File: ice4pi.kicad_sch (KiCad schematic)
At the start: 33 parts, among them J1 Conn_02x03, J2 Raspberry_Pi_2_3, J3 USB_C_Receptacle_USB2.0, J4 RJ45_Abracon_ARJP11A-MASA-B-A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, U1 ENC28J60x-SS, U2 DSC1001DE1-025.0000, U3 TPS2375-1

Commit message: fix: led
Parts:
- added R12: 332K, Resistor_SMD:R_0402_1005Metric, symbol Device:R
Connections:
- net LEDA: now also R6.1; no longer R7.1
- net LEDB: now also R7.1; no longer R6.1
- net at J4.11: now also R6.2; no longer R7.2
- net at J4.13: now also R7.2; no longer R6.2
- net at LSI-U1.6 (S2): now also R12.2; no longer U3.6 (PG)
- new net: R12.1, U3.6 (PG)
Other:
- moved on the sheet: R6, R7
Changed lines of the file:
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@@
 	(wire
 		(pts
-			(xy 106.68 96.52) (xy 113.03 96.52)
+			(xy 106.68 106.68) (xy 113.03 106.68)
 		)
 		(stroke
@@
 	(wire
 		(pts
-			(xy 96.52 106.68) (xy 99.06 106.68)
+			(xy 39.37 53.34) (xy 62.23 53.34)
 		)
 		(stroke
@@
 	(wire
 		(pts
-			(xy 39.37 53.34) (xy 62.23 53.34)
+			(xy 96.52 109.22) (xy 107.95 109.22)
 		)
 		(stroke
@@
 	(wire
 		(pts
-			(xy 107.95 99.06) (xy 96.52 99.06)
+			(xy 203.2 50.8) (xy 203.2 53.34)
 		)
 		(stroke
@@
 	(wire
 		(pts
-			(xy 203.2 50.8) (xy 203.2 53.34)
+			(xy 39.37 99.06) (xy 53.34 99.06)
 		)
 		(stroke
@@
 	(wire
 		(pts
-			(xy 39.37 99.06) (xy 53.34 99.06)
+			(xy 71.12 147.32) (xy 76.2 147.32)
 		)
 		(stroke
@@
 	(wire
 		(pts
-			(xy 71.12 147.32) (xy 76.2 147.32)
+			(xy 203.2 53.34) (xy 203.2 55.88)
 		)
 		(stroke
@@
 	(wire
 		(pts
-			(xy 203.2 53.34) (xy 203.2 55.88)
+			(xy 142.24 96.52) (xy 157.48 96.52)
 		)
 		(stroke
@@
 	(wire
 		(pts
-			(xy 142.24 96.52) (xy 157.48 96.52)
+			(xy 205.74 104.14) (xy 208.28 104.14)
 		)
 		(stroke
@@
 	(wire
 		(pts
+			(xy 96.52 99.06) (xy 107.95 99.06)
+		)
+		(stroke
+			(width 0)
+			(type default)
+		)
+	)
+	(wire
+		(pts
 			(xy 58.42 60.96) (xy 62.23 60.96)
 		)
@@
 	(wire
 		(pts
-			(xy 106.68 106.68) (xy 113.03 106.68)
+			(xy 106.68 96.52) (xy 113.03 96.52)
 		)
 		(stroke
@@
 	(wire
 		(pts
-			(xy 96.52 96.52) (xy 99.06 96.52)
-		)
-		(stroke
-			(width 0)
-			(type default)
-		)
-	)
-	(wire
-		(pts
 			(xy 203.2 45.72) (xy 203.2 48.26)
 		)
@@
 	(wire
 		(pts
+			(xy 96.52 106.68) (xy 99.06 106.68)
+		)
+		(stroke
+			(width 0)
+			(type default)
+		)
+	)
+	(wire
+		(pts
 			(xy 58.42 148.59) (xy 58.42 149.86)
 		)
@@
 	(wire
 		(pts
-			(xy 107.95 109.22) (xy 96.52 109.22)
-		)
-		(stroke
-			(width 0)
-			(type default)
-		)
-	)
-	(wire
-		(pts
 			(xy 203.2 43.18) (xy 203.2 45.72)
 		)
@@
 	(wire
 		(pts
-			(xy 195.58 104.14) (xy 208.28 104.14)
+			(xy 195.58 104.14) (xy 198.12 104.14)
 		)
 		(stroke
@@
 		)
 	)
+	(wire
+		(pts
+			(xy 96.52 96.52) (xy 99.06 96.52)
+		)
+		(stroke
+			(width 0)
+			(type default)
+		)
+	)
 	(text_box "INTERFACE"
 		(exclude_from_sim no)
@@
 		)
 	)
-	(label "LEDB"
-		(at 107.95 96.52 0)
+	(label "LEDA"
+		(at 109.22 106.68 0)
 		(fields_autoplaced yes)
 		(effects
@@
 		)
 	)
-	(label "LEDA"
-		(at 107.95 106.68 0)
+	(label "LEDB"
+		(at 109.22 96.52 0)
 		(fields_autoplaced yes)
 		(effects
@@
 	(symbol
 		(lib_id "power:GND")
-		(at 107.95 99.06 90)
+		(at 107.95 109.22 90)
 		(unit 1)
 		(exclude_from_sim no)
@@
 		(dnp no)
 		(property "Reference" "#PWR06"
-			(at 114.3 99.06 0)
+			(at 114.3 109.22 0)
 			(effects
 				(font
@@
 		)
 		(property "Value" "GND"
-			(at 110.49 97.79 90)
+			(at 110.49 107.95 90)
 			(effects
 				(font
@@
 		)
 		(property "Footprint" ""
-			(at 107.95 99.06 0)
+			(at 107.95 109.22 0)
 			(effects
 				(font
@@
 		)
 		(property "Datasheet" ""
-			(at 107.95 99.06 0)
+			(at 107.95 109.22 0)
 			(effects
 				(font
@@
 		)
 		(property "Description" ""
-			(at 107.95 99.06 0)
+			(at 107.95 109.22 0)
 			(effects
 				(font
@@
 	(symbol
 		(lib_id "Device:R")
-		(at 102.87 106.68 270)
+		(at 102.87 96.52 270)
 		(unit 1)
 		(exclude_from_sim no)
@@
 		(dnp no)
 		(property "Reference" "R7"
-			(at 106.68 105.41 90)
+			(at 106.68 95.25 90)
 			(effects
 				(font
@@
 		)
 		(property "Value" "1K"
-			(at 99.06 107.95 90)
+			(at 99.06 97.79 90)
 			(effects
 				(font
@@
 		)
 		(property "Footprint" "Resistor_SMD:R_0402_1005Metric"
-			(at 102.87 104.902 90)
+			(at 102.87 94.742 90)
 			(effects
 				(font
@@
 		)
 		(property "Datasheet" "~"
-			(at 102.87 106.68 0)
+			(at 102.87 96.52 0)
 			(effects
 				(font
@@
 		)
 		(property "Description" ""
-			(at 102.87 106.68 0)
+			(at 102.87 96.52 0)
 			(effects
 				(font
@@
 	(symbol
 		(lib_id "power:GND")
-		(at 107.95 109.22 90)
+		(at 107.95 99.06 90)
 		(unit 1)
 		(exclude_from_sim no)
@@
 		(dnp no)
 		(property "Reference" "#PWR05"
-			(at 114.3 109.22 0)
+			(at 114.3 99.06 0)
 			(effects
 				(font
@@
 		)
 		(property "Value" "GND"
-			(at 110.49 107.95 90)
+			(at 110.49 97.79 90)
 			(effects
 				(font
@@
 		)
 		(property "Footprint" ""
-			(at 107.95 109.22 0)
+			(at 107.95 99.06 0)
 			(effects
 				(font
@@
 		)
 		(property "Datasheet" ""
-			(at 107.95 109.22 0)
+			(at 107.95 99.06 0)
 			(effects
 				(font
@@
 		)
 		(property "Description" ""
-			(at 107.95 109.22 0)
+			(at 107.95 99.06 0)
 			(effects
 				(font
@@
 	(symbol
 		(lib_id "Device:R")
+		(at 201.93 104.14 90)
+		(unit 1)
+		(exclude_from_sim no)
+		(in_bom yes)
+		(on_board yes)
+		(dnp no)
+		(property "Reference" "R12"
+			(at 201.93 101.854 90)
+			(effects
+				(font
+					(size 1.27 1.27)
+				)
+			)
+		)
+		(property "Value" "332K"
+			(at 201.93 106.172 90)
+			(effects
+				(font
+					(size 1.27 1.27)
+				)
+			)
+		)
+		(property "Footprint" "Resistor_SMD:R_0402_1005Metric"
+			(at 201.93 105.918 90)
+			(effects
+				(font
+					(size 1.27 1.27)
+				)
+				(hide yes)
+			)
+		)
+		(property "Datasheet" "~"
+			(at 201.93 104.14 0)
+			(effects
+				(font
+					(size 1.27 1.27)
+				)
+				(hide yes)
+			)
+		)
+		(property "Description" "Resistor"
+			(at 201.93 104.14 0)
+			(effects
+				(font
+					(size 1.27 1.27)
+				)
+				(hide yes)
+			)
+		)
+		(pin "2"
+		)
+		(pin "1"
+		)
+		(instances
+			(project ""
+				(path "/0f54db53-a272-4955-88fb-d7ab00657bb0"
+					(reference "R12")
+					(unit 1)
+				)
+			)
+		)
+	)
+	(symbol
+		(lib_id "Device:R")
 		(at 43.18 101.6 90)
 		(unit 1)
@@
 	(symbol
 		(lib_id "Device:R")
-		(at 102.87 96.52 270)
+		(at 102.87 106.68 270)
 		(unit 1)
 		(exclude_from_sim no)
@@
 		(dnp no)
 		(property "Reference" "R6"
-			(at 106.68 95.25 90)
+			(at 106.68 105.41 90)
 			(effects
 				(font
@@
 		)
 		(property "Value" "1K"
-			(at 99.06 97.79 90)
+			(at 99.06 107.95 90)
 			(effects
 				(font
@@
 		)
 		(property "Footprint" "Resistor_SMD:R_0402_1005Metric"
-			(at 102.87 94.742 90)
+			(at 102.87 104.902 90)
 			(effects
 				(font
@@
 		)
 		(property "Datasheet" "~"
-			(at 102.87 96.52 0)
+			(at 102.87 106.68 0)
 			(effects
 				(font
@@
 		)
 		(property "Description" ""
-			(at 102.87 96.52 0)
+			(at 102.87 106.68 0)
 			(effects
 				(font

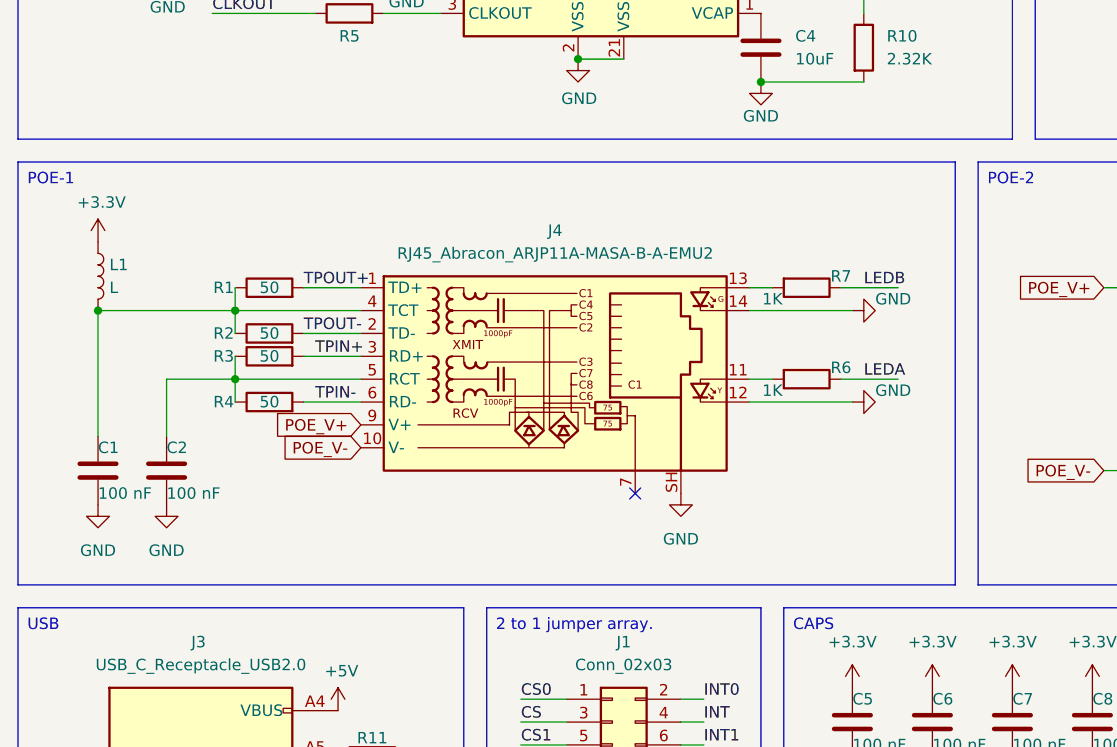
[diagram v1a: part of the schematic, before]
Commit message: fix: fixed led polarity
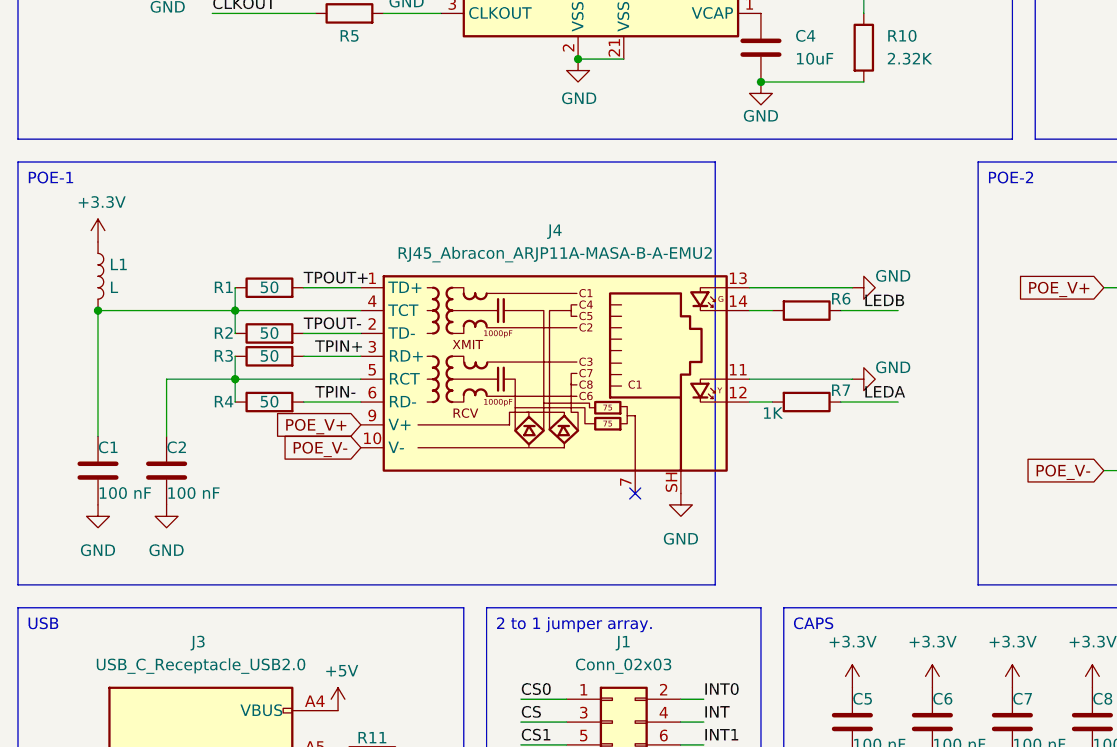
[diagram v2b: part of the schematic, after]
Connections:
- net GND: now also J4.11, J4.13; no longer J4.12, J4.14
- net LEDA: now also R7.1; no longer R6.1
- net LEDB: now also R6.1; no longer R7.1
- net at R6.2: now also J4.14; no longer J4.11
- net at R7.2: now also J4.12; no longer J4.13
